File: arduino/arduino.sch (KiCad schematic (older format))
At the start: 8 parts

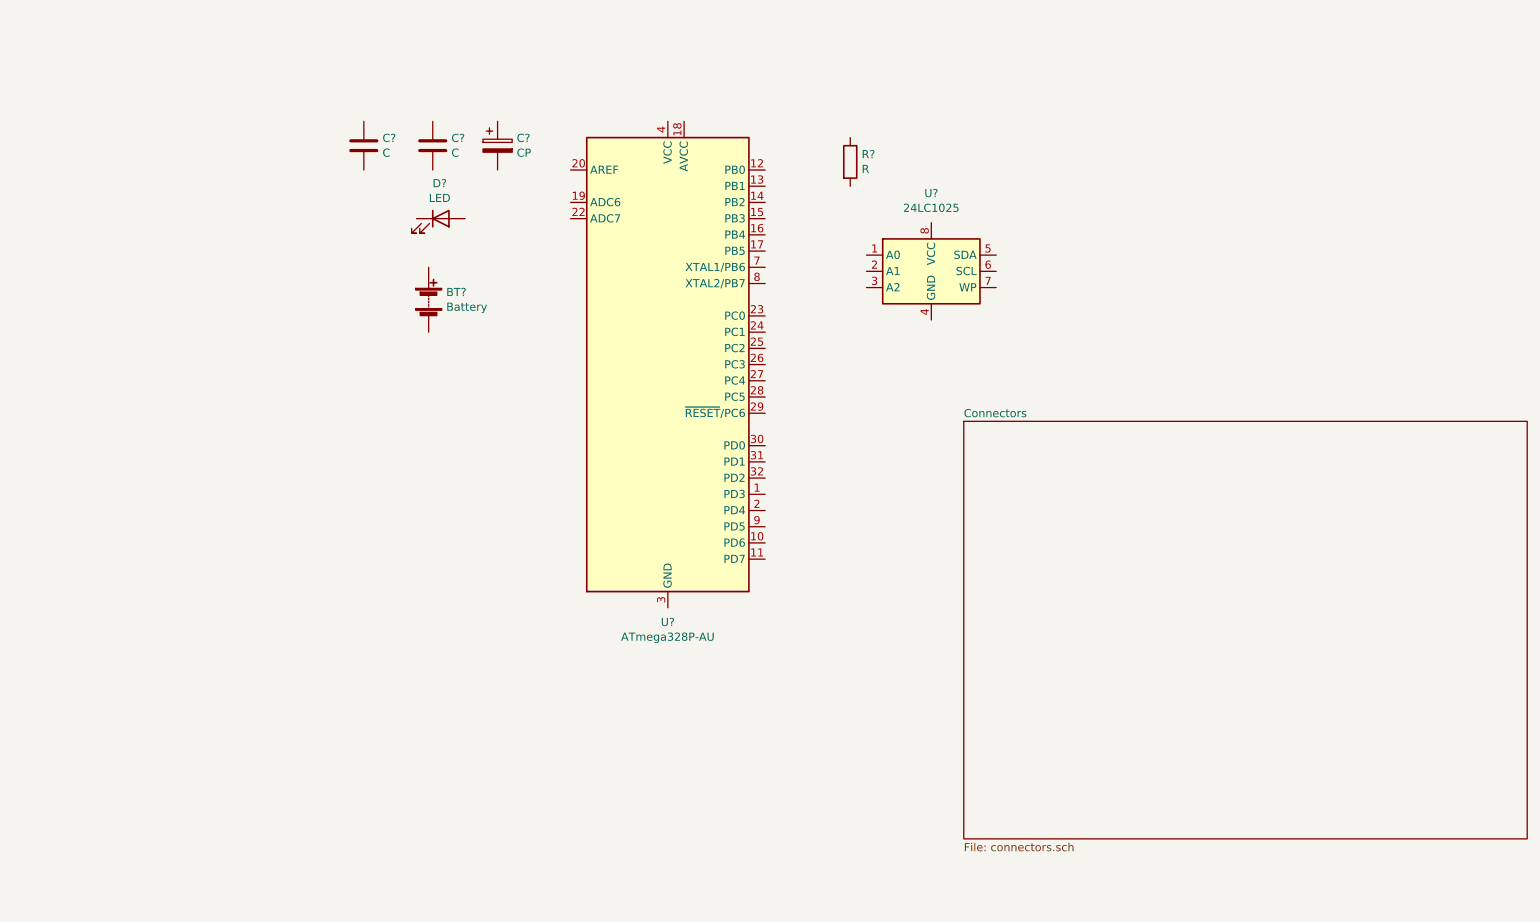
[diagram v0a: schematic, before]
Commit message: Create component + add
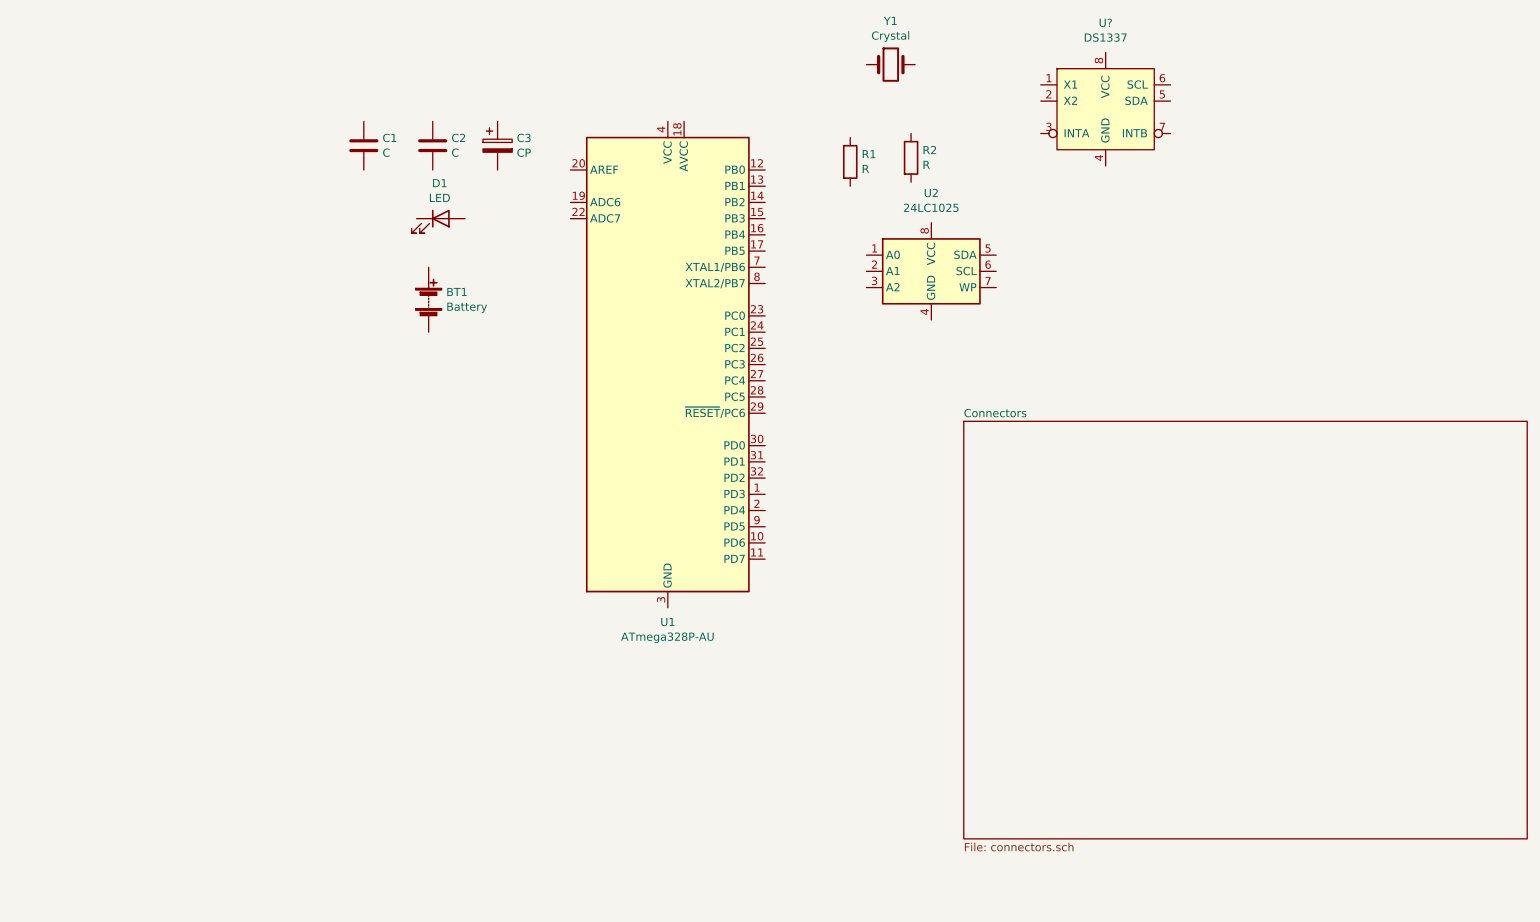
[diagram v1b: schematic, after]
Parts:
- added R2: R, Resistor_SMD:R_0805_2012Metric, symbol Device:R
- added U?: DS1337, symbol Zeko369:DS1337
- added Y1: Crystal, symbol Device:Crystal
- C1, C2: renamed from C?; footprint (none) -> Capacitor_SMD:C_0805_2012Metric
- D1: renamed from D?; footprint (none) -> LED_SMD:LED_0805_2012Metric
- R1: renamed from R?; footprint (none) -> Resistor_SMD:R_0805_2012Metric
- U2: renamed from U?; footprint (none) -> Package_SO:SOIC-8_3.9x4.9mm_P1.27mm
- gave numbers to parts that had none: 3
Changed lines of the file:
@@
 $EndDescr
 $Comp
-L MCU_Microchip_ATmega:ATmega328P-AU U?
+L MCU_Microchip_ATmega:ATmega328P-AU U1
 U 1 1 6172B6ED
 P 5700 3525
-F 0 "U?" H 5700 1936 50  0000 C CNN
+F 0 "U1" H 5700 1936 50  0000 C CNN
 F 1 "ATmega328P-AU" H 5700 1845 50  0000 C CNN
 F 2 "Package_QFP:TQFP-32_7x7mm_P0.8mm" H 5700 3525 50  0001 C CIN
@@
 $EndComp
 $Comp
-L Device:Battery BT?
+L Device:Battery BT1
 U 1 1 6172D370
 P 4225 3125
-F 0 "BT?" H 4333 3171 50  0000 L CNN
+F 0 "BT1" H 4333 3171 50  0000 L CNN
 F 1 "Battery" H 4333 3080 50  0000 L CNN
 F 2 "" V 4225 3185 50  0001 C CNN
@@
 $EndComp
 $Comp
-L Device:C C?
+L Device:C C2
 U 1 1 6172E0FB
 P 4250 2175
-F 0 "C?" H 4365 2221 50  0000 L CNN
+F 0 "C2" H 4365 2221 50  0000 L CNN
 F 1 "C" H 4365 2130 50  0000 L CNN
-F 2 "" H 4288 2025 50  0001 C CNN
+F 2 "Capacitor_SMD:C_0805_2012Metric" H 4288 2025 50  0001 C CNN
 F 3 "~" H 4250 2175 50  0001 C CNN
 	1    4250 2175
@@
 $EndComp
 $Comp
-L Device:CP C?
+L Device:CP C3
 U 1 1 6172E61F
 P 4650 2175
-F 0 "C?" H 4768 2221 50  0000 L CNN
+F 0 "C3" H 4768 2221 50  0000 L CNN
 F 1 "CP" H 4768 2130 50  0000 L CNN
 F 2 "" H 4688 2025 50  0001 C CNN
@@
 $EndComp
 $Comp
-L Device:LED D?
+L Device:LED D1
 U 1 1 6172EEA0
 P 4300 2625
-F 0 "D?" H 4293 2842 50  0000 C CNN
+F 0 "D1" H 4293 2842 50  0000 C CNN
 F 1 "LED" H 4293 2751 50  0000 C CNN
-F 2 "" H 4300 2625 50  0001 C CNN
+F 2 "LED_SMD:LED_0805_2012Metric" H 4300 2625 50  0001 C CNN
 F 3 "~" H 4300 2625 50  0001 C CNN
 	1    4300 2625
@@
 $EndComp
 $Comp
-L Device:R R?
+L Device:R R1
 U 1 1 61732E28
 P 6825 2275
-F 0 "R?" H 6895 2321 50  0000 L CNN
+F 0 "R1" H 6895 2321 50  0000 L CNN
 F 1 "R" H 6895 2230 50  0000 L CNN
-F 2 "" V 6755 2275 50  0001 C CNN
+F 2 "Resistor_SMD:R_0805_2012Metric" V 6755 2275 50  0001 C CNN
 F 3 "~" H 6825 2275 50  0001 C CNN
 	1    6825 2275
@@
 $EndComp
 $Comp
-L Memory_EEPROM:24LC1025 U?
+L Memory_EEPROM:24LC1025 U2
 U 1 1 61733EC2
 P 7325 2950
-F 0 "U?" H 7325 3431 50  0000 C CNN
+F 0 "U2" H 7325 3431 50  0000 C CNN
 F 1 "24LC1025" H 7325 3340 50  0000 C CNN
-F 2 "" H 7325 2950 50  0001 C CNN
+F 2 "Package_SO:SOIC-8_3.9x4.9mm_P1.27mm" H 7325 2950 50  0001 C CNN
 F 3 "http://ww1.microchip.com/downloads/en/DeviceDoc/21941B.pdf" H 7325 2950 50  0001 C CNN
 	1    7325 2950
@@
 $EndComp
 $Comp
-L Device:C C?
+L Device:C C1
 U 1 1 61737550
 P 3825 2175
-F 0 "C?" H 3940 2221 50  0000 L CNN
+F 0 "C1" H 3940 2221 50  0000 L CNN
 F 1 "C" H 3940 2130 50  0000 L CNN
-F 2 "" H 3863 2025 50  0001 C CNN
+F 2 "Capacitor_SMD:C_0805_2012Metric" H 3863 2025 50  0001 C CNN
 F 3 "~" H 3825 2175 50  0001 C CNN
 	1    3825 2175
@@
 F1 "connectors.sch" 50
 $EndSheet
+$Comp
+L Device:R R2
+U 1 1 617410C7
+P 7200 2250
+F 0 "R2" H 7270 2296 50  0000 L CNN
+F 1 "R" H 7270 2205 50  0000 L CNN
+F 2 "Resistor_SMD:R_0805_2012Metric" V 7130 2250 50  0001 C CNN
+F 3 "~" H 7200 2250 50  0001 C CNN
+	1    7200 2250
+	1    0    0    -1
+$EndComp
+$Comp
+L Device:Crystal Y1
+U 1 1 61742D86
+P 7075 1675
+F 0 "Y1" H 7075 1943 50  0000 C CNN
+F 1 "Crystal" H 7075 1852 50  0000 C CNN
+F 2 "" H 7075 1675 50  0001 C CNN
+F 3 "~" H 7075 1675 50  0001 C CNN
+	1    7075 1675
+	1    0    0    -1
+$EndComp
+$Comp
+L Zeko369:DS1337 U?
+U 1 1 61745381
+P 8400 1950
+F 0 "U?" H 8400 2481 50  0000 C CNN
+F 1 "DS1337" H 8400 2390 50  0000 C CNN
+F 2 "" H 8400 1950 50  0001 C CNN
+F 3 "" H 8400 1950 50  0001 C CNN
+	1    8400 1950
+	1    0    0    -1
+$EndComp
 $EndSCHEMATC

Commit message: Add component values
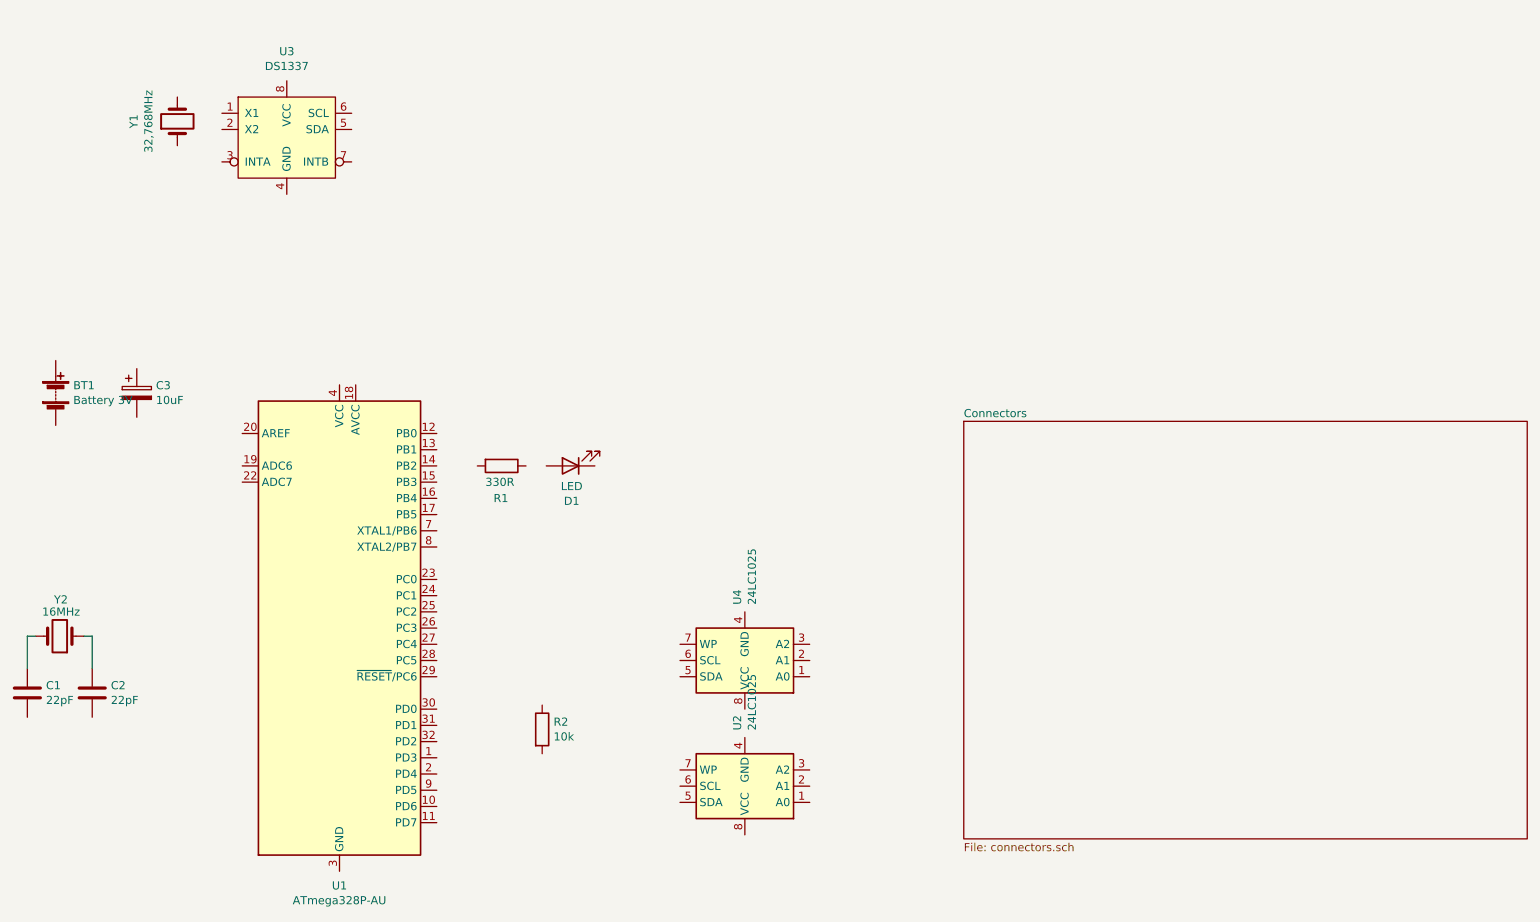
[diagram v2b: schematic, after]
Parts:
- added U4: 24LC1025, Package_SO:SOIC-8_3.9x4.9mm_P1.27mm, symbol Memory_EEPROM:24LC1025
- added Y2: 16MHz, Crystal:Crystal_SMD_5032-2Pin_5.0x3.2mm, symbol Device:Crystal
- BT1: value Battery -> Battery 3V; footprint (none) -> Connector_PinSocket_2.54mm:PinSocket_1x02_P2.54mm_Vertical
- C1, C2: value C -> 22pF
- C3: value CP -> 10uF; footprint (none) -> Capacitor_SMD:CP_Elec_4x3
- R1: value R -> 330R
- R2: value R -> 10k
- U3: renamed from U?; footprint (none) -> Package_SO:SO-8_5.3x6.2mm_P1.27mm
- Y1: value Crystal -> 32,768MHz; footprint (none) -> Crystal:Crystal_SMD_MicroCrystal_CC7V-T1A-2Pin_3.2x1.5mm
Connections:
- net at C2.1: now also Y2.1
- net at C1.1: now also Y2.2
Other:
- moved on the sheet: BT1, C1, C2, C3, D1, R1, R2, U1, U2, U3, Y1
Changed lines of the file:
@@
 L MCU_Microchip_ATmega:ATmega328P-AU U1
 U 1 1 6172B6ED
-P 5700 3525
-F 0 "U1" H 5700 1936 50  0000 C CNN
-F 1 "ATmega328P-AU" H 5700 1845 50  0000 C CNN
-F 2 "Package_QFP:TQFP-32_7x7mm_P0.8mm" H 5700 3525 50  0001 C CIN
-F 3 "http://ww1.microchip.com/downloads/en/DeviceDoc/ATmega328_P%20AVR%20MCU%20with%20picoPower%20Technology%20Data%20Sheet%2040001984A.pdf" H 5700 3525 50  0001 C CNN
-	1    5700 3525
+P 3675 5150
+F 0 "U1" H 3675 3561 50  0000 C CNN
+F 1 "ATmega328P-AU" H 3675 3470 50  0000 C CNN
+F 2 "Package_QFP:TQFP-32_7x7mm_P0.8mm" H 3675 5150 50  0001 C CIN
+F 3 "http://ww1.microchip.com/downloads/en/DeviceDoc/ATmega328_P%20AVR%20MCU%20with%20picoPower%20Technology%20Data%20Sheet%2040001984A.pdf" H 3675 5150 50  0001 C CNN
+	1    3675 5150
 	1    0    0    -1
 $EndComp
@@
 L Device:Battery BT1
 U 1 1 6172D370
-P 4225 3125
-F 0 "BT1" H 4333 3171 50  0000 L CNN
-F 1 "Battery" H 4333 3080 50  0000 L CNN
-F 2 "" V 4225 3185 50  0001 C CNN
-F 3 "~" V 4225 3185 50  0001 C CNN
-	1    4225 3125
+P 1925 3700
+F 0 "BT1" H 2033 3746 50  0000 L CNN
+F 1 "Battery 3V" H 2033 3655 50  0000 L CNN
+F 2 "Connector_PinSocket_2.54mm:PinSocket_1x02_P2.54mm_Vertical" V 1925 3760 50  0001 C CNN
+F 3 "~" V 1925 3760 50  0001 C CNN
+	1    1925 3700
 	1    0    0    -1
 $EndComp
@@
 L Device:C C2
 U 1 1 6172E0FB
-P 4250 2175
-F 0 "C2" H 4365 2221 50  0000 L CNN
-F 1 "C" H 4365 2130 50  0000 L CNN
-F 2 "Capacitor_SMD:C_0805_2012Metric" H 4288 2025 50  0001 C CNN
-F 3 "~" H 4250 2175 50  0001 C CNN
-	1    4250 2175
+P 2150 5550
+F 0 "C2" H 2265 5596 50  0000 L CNN
+F 1 "22pF" H 2265 5505 50  0000 L CNN
+F 2 "Capacitor_SMD:C_0805_2012Metric" H 2188 5400 50  0001 C CNN
+F 3 "~" H 2150 5550 50  0001 C CNN
+	1    2150 5550
 	1    0    0    -1
 $EndComp
@@
 L Device:CP C3
 U 1 1 6172E61F
-P 4650 2175
-F 0 "C3" H 4768 2221 50  0000 L CNN
-F 1 "CP" H 4768 2130 50  0000 L CNN
-F 2 "" H 4688 2025 50  0001 C CNN
-F 3 "~" H 4650 2175 50  0001 C CNN
-	1    4650 2175
+P 2425 3700
+F 0 "C3" H 2543 3746 50  0000 L CNN
+F 1 "10uF" H 2543 3655 50  0000 L CNN
+F 2 "Capacitor_SMD:CP_Elec_4x3" H 2463 3550 50  0001 C CNN
+F 3 "~" H 2425 3700 50  0001 C CNN
+	1    2425 3700
 	1    0    0    -1
 $EndComp
@@
 L Device:LED D1
 U 1 1 6172EEA0
-P 4300 2625
-F 0 "D1" H 4293 2842 50  0000 C CNN
-F 1 "LED" H 4293 2751 50  0000 C CNN
-F 2 "LED_SMD:LED_0805_2012Metric" H 4300 2625 50  0001 C CNN
-F 3 "~" H 4300 2625 50  0001 C CNN
-	1    4300 2625
-	1    0    0    -1
+P 5100 4150
+F 0 "D1" H 5093 4367 50  0000 C CNN
+F 1 "LED" H 5093 4276 50  0000 C CNN
+F 2 "LED_SMD:LED_0805_2012Metric" H 5100 4150 50  0001 C CNN
+F 3 "~" H 5100 4150 50  0001 C CNN
+	1    5100 4150
+	-1   0    0    1
 $EndComp
 $Comp
 L Device:R R1
 U 1 1 61732E28
-P 6825 2275
-F 0 "R1" H 6895 2321 50  0000 L CNN
-F 1 "R" H 6895 2230 50  0000 L CNN
-F 2 "Resistor_SMD:R_0805_2012Metric" V 6755 2275 50  0001 C CNN
-F 3 "~" H 6825 2275 50  0001 C CNN
-	1    6825 2275
-	1    0    0    -1
+P 4675 4150
+F 0 "R1" V 4875 4100 50  0000 L CNN
+F 1 "330R" V 4775 4050 50  0000 L CNN
+F 2 "Resistor_SMD:R_0805_2012Metric" V 4605 4150 50  0001 C CNN
+F 3 "~" H 4675 4150 50  0001 C CNN
+	1    4675 4150
+	0    1    1    0
 $EndComp
 $Comp
 L Memory_EEPROM:24LC1025 U2
 U 1 1 61733EC2
-P 7325 2950
-F 0 "U2" H 7325 3431 50  0000 C CNN
-F 1 "24LC1025" H 7325 3340 50  0000 C CNN
-F 2 "Package_SO:SOIC-8_3.9x4.9mm_P1.27mm" H 7325 2950 50  0001 C CNN
-F 3 "http://ww1.microchip.com/downloads/en/DeviceDoc/21941B.pdf" H 7325 2950 50  0001 C CNN
-	1    7325 2950
-	1    0    0    -1
+P 6175 6125
+F 0 "U2" V 6221 5781 50  0000 R CNN
+F 1 "24LC1025" V 6130 5781 50  0000 R CNN
+F 2 "Package_SO:SOIC-8_3.9x4.9mm_P1.27mm" H 6175 6125 50  0001 C CNN
+F 3 "http://ww1.microchip.com/downloads/en/DeviceDoc/21941B.pdf" H 6175 6125 50  0001 C CNN
+	1    6175 6125
+	-1   0    0    1
 $EndComp
 $Comp
 L Device:C C1
 U 1 1 61737550
-P 3825 2175
-F 0 "C1" H 3940 2221 50  0000 L CNN
-F 1 "C" H 3940 2130 50  0000 L CNN
-F 2 "Capacitor_SMD:C_0805_2012Metric" H 3863 2025 50  0001 C CNN
-F 3 "~" H 3825 2175 50  0001 C CNN
-	1    3825 2175
+P 1750 5550
+F 0 "C1" H 1865 5596 50  0000 L CNN
+F 1 "22pF" H 1865 5505 50  0000 L CNN
+F 2 "Capacitor_SMD:C_0805_2012Metric" H 1788 5400 50  0001 C CNN
+F 3 "~" H 1750 5550 50  0001 C CNN
+	1    1750 5550
 	1    0    0    -1
 $EndComp
@@
 L Device:R R2
 U 1 1 617410C7
-P 7200 2250
-F 0 "R2" H 7270 2296 50  0000 L CNN
-F 1 "R" H 7270 2205 50  0000 L CNN
-F 2 "Resistor_SMD:R_0805_2012Metric" V 7130 2250 50  0001 C CNN
-F 3 "~" H 7200 2250 50  0001 C CNN
-	1    7200 2250
+P 4925 5775
+F 0 "R2" H 4995 5821 50  0000 L CNN
+F 1 "10k" H 4995 5730 50  0000 L CNN
+F 2 "Resistor_SMD:R_0805_2012Metric" V 4855 5775 50  0001 C CNN
+F 3 "~" H 4925 5775 50  0001 C CNN
+	1    4925 5775
 	1    0    0    -1
 $EndComp
@@
 L Device:Crystal Y1
 U 1 1 61742D86
-P 7075 1675
-F 0 "Y1" H 7075 1943 50  0000 C CNN
-F 1 "Crystal" H 7075 1852 50  0000 C CNN
-F 2 "" H 7075 1675 50  0001 C CNN
-F 3 "~" H 7075 1675 50  0001 C CNN
-	1    7075 1675
+P 2675 2025
+F 0 "Y1" H 2675 2293 50  0000 C CNN
+F 1 "32,768MHz" H 2675 2202 50  0000 C CNN
+F 2 "Crystal:Crystal_SMD_MicroCrystal_CC7V-T1A-2Pin_3.2x1.5mm" H 2675 2025 50  0001 C CNN
+F 3 "~" H 2675 2025 50  0001 C CNN
+	1    2675 2025
+	0    -1   -1   0
+$EndComp
+$Comp
+L Zeko369:DS1337 U3
+U 1 1 61745381
+P 3350 2125
+F 0 "U3" H 3350 2656 50  0000 C CNN
+F 1 "DS1337" H 3350 2565 50  0000 C CNN
+F 2 "Package_SO:SO-8_5.3x6.2mm_P1.27mm" H 3350 2125 50  0001 C CNN
+F 3 "" H 3350 2125 50  0001 C CNN
+	1    3350 2125
 	1    0    0    -1
 $EndComp
 $Comp
-L Zeko369:DS1337 U?
-U 1 1 61745381
-P 8400 1950
-F 0 "U?" H 8400 2481 50  0000 C CNN
-F 1 "DS1337" H 8400 2390 50  0000 C CNN
-F 2 "" H 8400 1950 50  0001 C CNN
-F 3 "" H 8400 1950 50  0001 C CNN
-	1    8400 1950
-	1    0    0    -1
+L Device:Crystal Y2
+U 1 1 61745F91
+P 1950 5200
+F 0 "Y2" H 1900 4975 50  0000 L CNN
+F 1 "16MHz" H 1825 5050 50  0000 L CNN
+F 2 "Crystal:Crystal_SMD_5032-2Pin_5.0x3.2mm" H 1950 5200 50  0001 C CNN
+F 3 "~" H 1950 5200 50  0001 C CNN
+	1    1950 5200
+	-1   0    0    1
 $EndComp
+$Comp
+L Memory_EEPROM:24LC1025 U4
+U 1 1 61748B0D
+P 6175 5350
+F 0 "U4" V 6221 5006 50  0000 R CNN
+F 1 "24LC1025" V 6130 5006 50  0000 R CNN
+F 2 "Package_SO:SOIC-8_3.9x4.9mm_P1.27mm" H 6175 5350 50  0001 C CNN
+F 3 "http://ww1.microchip.com/downloads/en/DeviceDoc/21941B.pdf" H 6175 5350 50  0001 C CNN
+	1    6175 5350
+	-1   0    0    1
+$EndComp
+Wire Wire Line
+	1750 5400 1750 5200
+Wire Wire Line
+	1750 5200 1800 5200
+Wire Wire Line
+	2150 5400 2150 5200
+Wire Wire Line
+	2150 5200 2100 5200
 $EndSCHEMATC

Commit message: Done with schematic, start PCB
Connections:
- net D3: now reaches U1.1 (PD3)
- net D6: now reaches U1.10 (PD6)
- net D7: now reaches U1.11 (PD7)
- net D8: now reaches U1.12 (PB0)
- net MOSI: now reaches U1.15 (PB3)
- net MISO: now reaches U1.16 (PB4)
- net at U1.17 (PB5): now also R1.2
- net VCC: now reaches U1.18 (AVCC)
- net VCC: now also BT1.1 (+), C3.1, R2.1, U1.20 (AREF), U1.4 (VCC), U1.6 (VCC), U2.8 (VCC), U3.3 (INTA), U3.8 (VCC), U4.8 (VCC)
- net D4: now reaches U1.2 (PD4)
- net GND: now reaches U1.21 (GND), U1.3 (GND), U1.5 (GND)
- net GND: now also BT1.2 (-), C1.2, C2.2, C3.2, D1.1 (K), U2.3 (A2), U2.4 (GND), U2.7 (WP), U3.4 (GND), U4.3 (A2), U4.4 (GND), U4.7 (WP)
- net ADDS1: now reaches U1.23 (PC0)
- net ADDS1: now also U2.1 (A0), U4.1 (A0)
- net ADDS2: now reaches U1.24 (PC1)
- net ADDS2: now also U2.2 (A1), U4.2 (A1)
- net SDA: now reaches U1.27 (PC4)
- net SDA: now also U2.5 (SDA), U3.5 (SDA), U4.5 (SDA)
- net SCL: now reaches U1.28 (PC5)
- net SCL: now also U2.6 (SCL), U3.6 (SCL), U4.6 (SCL)
- net RST: now reaches U1.29 (~RESET~/PC6)
- net RST: now also R2.2
- net RX: now reaches U1.30 (PD0)
- net TX: now reaches U1.31 (PD1)
- net D2: now reaches U1.32 (PD2)
- net X1: now reaches U1.7 (XTAL1/PB6)
- net X1: now also C1.1, Y2.2
- net X2: now reaches U1.8 (XTAL2/PB7)
- net X2: now also C2.1, Y2.1
- net D5: now reaches U1.9 (PD5)
- net at D1.2 (A): now also R1.1
- net at Y1.1: now also U3.2 (X2)
- net at Y1.2: now also U3.1 (X1)
- no-connect marks 0 -> 7
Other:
- moved on the sheet: BT1, D1, R1, R2, U2, U4

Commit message: Layout setup
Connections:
- net GND: no longer U2.3 (A2), U4.3 (A2)
- net VCC: now also U2.3 (A2), U4.3 (A2)
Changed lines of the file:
@@
 	5375 3750 5775 3750
-Wire Wire Line
-	6050 3750 6225 3750
 Wire Wire Line
 	5775 3550 5775 3750
@@
 ADDS2
 Wire Wire Line
-	4975 3550 4925 3550
-Wire Wire Line
-	4925 3550 4925 3750
-Wire Wire Line
 	4925 3750 5375 3750
 Connection ~ 5375 3750
-Wire Wire Line
-	6275 3550 6225 3550
-Wire Wire Line
-	6225 3550 6225 3750
-Connection ~ 6225 3750
-Wire Wire Line
-	6225 3750 6675 3750
 Wire Wire Line
 	3075 3950 3075 3550
@@
 	0    -1   -1   0
 $EndComp
+Wire Wire Line
+	6050 3750 6675 3750
+Text Label 4750 3550 0    50   ~ 0
+VCC
+Text Label 6050 3550 0    50   ~ 0
+VCC
+Wire Wire Line
+	6050 3550 6275 3550
+Wire Wire Line
+	4750 3550 4975 3550
 $EndSCHEMATC

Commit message: Finish course
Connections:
- net ADDS1: now also U1.24 (PC1); no longer U1.23 (PC0)
- net ADDS2: now also U1.23 (PC0); no longer U1.24 (PC1)
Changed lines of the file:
@@
 ADDS2
 Text Label 4550 4850 2    50   ~ 0
+ADDS2
+Text Label 4550 4950 2    50   ~ 0
 ADDS1
-Text Label 4550 4950 2    50   ~ 0
-ADDS2
 Wire Wire Line
 	4275 4850 4550 4850
